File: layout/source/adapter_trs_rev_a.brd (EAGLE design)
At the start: 200 x 50 mm, 81 parts, among them IC1 STM32F103C8T, IC2 LP2985-SOT23-5, IC3 IC_USBLC6-2, IC4 IC_USBLC6-2, IC5 LT1619ES8, IC6 LP2985-SOT23-5, IC7 IRF7470, SW1 2P2T, T1 LPISR, Y1 532-CRYSTAL, Y2 EQ161-CRYSTAL

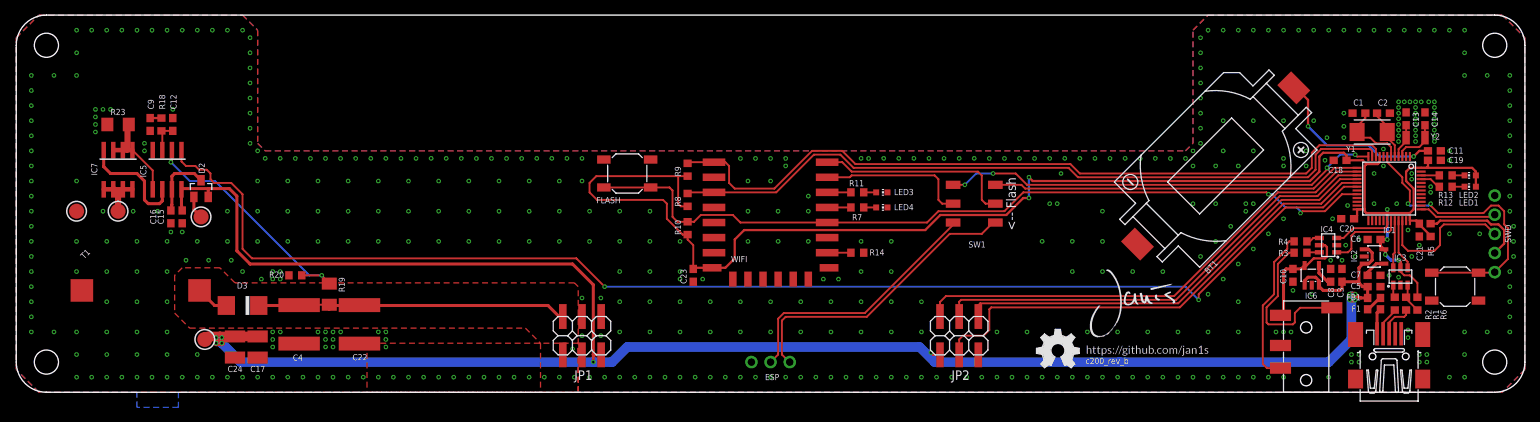
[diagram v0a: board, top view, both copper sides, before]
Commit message: Added new control board versions and TRS adapter
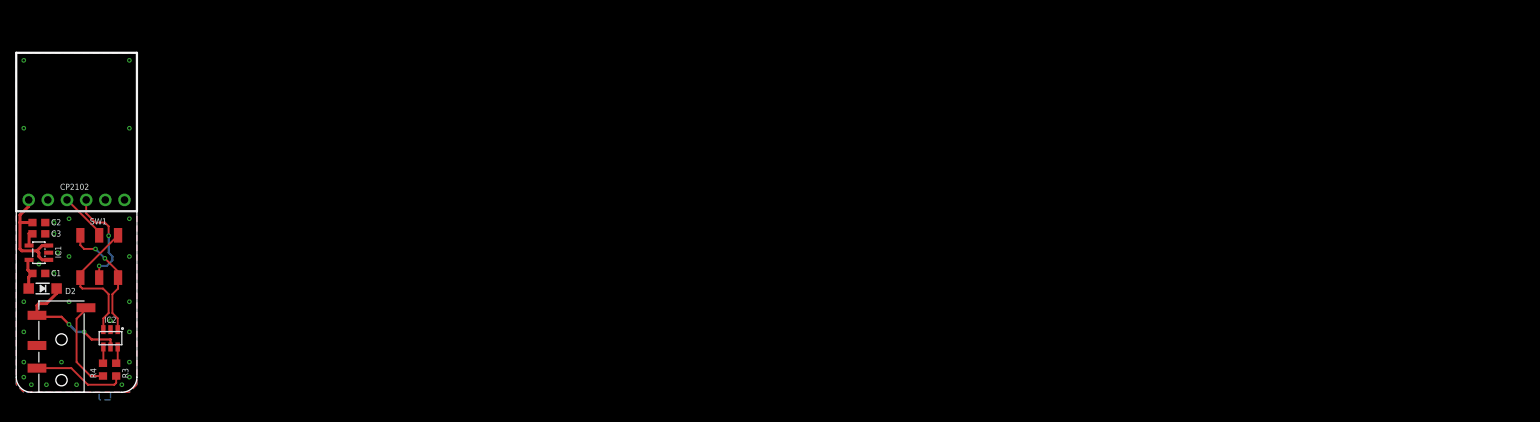
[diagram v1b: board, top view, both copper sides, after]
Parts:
- removed BT1: CR2032-HOLDER, battery-holder:CH28-2032LF
- removed C10, C11, C5, C6: 10µF/6.3V, rcl:C0603
- removed C12: 22nF, rcl:C0603
- removed C13, C14: 10p, rcl:C0603
- removed C15, C16: 10µF, rcl:C0603
- removed C17, C24: 100µF/6.3V, rcl:C1210
- removed C18, C23: 1µF, rcl:C0603
- removed C19, C20, C21: 100nF, rcl:C0603
- removed C22, C4: 1µF/250V, rcl:C2220K
- removed C7, C8: 10nF, rcl:C0603
- removed C9: 150pF, rcl:C0603
- removed D3: ES2, diode:DO-214AA
- removed ESP: (no value), microbuilder:1X03_ROUND
- removed F1, R12, R13: 1k, rcl:R0603
- removed FB1: EMI, rcl:R0603
- removed FLASH, ISP: TACT-SWITCH-40-40, tactile-switch:40-40
- removed IC3, IC4: IC_USBLC6-2, dp_devices:SOT-23-6L
- removed IC5: LT1619ES8, lt:SO8
- removed IC6: LP2985-SOT23-5, vreg:SOT23-5
- removed IC7: IRF7470, ir:SO8
- removed JP1, JP2: (no value), con-pinhead:2X03SMD
- removed LED1, LED2, LED3, LED4: (no value), led:CHIP-LED0603
- removed LOGO1, LOGO2: OSHW_LOGO_FILLX0200-NT, ohw-logo:OSHW_FILLX200_NOTEXT
- removed R1, R2, R5: 33R, rcl:R0603
- removed R10, R11, R14, R7, R8, R9: 10k, rcl:R0603
- removed R18: 82k, rcl:R0603
- removed R19: 1M, rcl:M1206
- removed R20: 8k2, rcl:R0603
- removed R23: 0.01R, rcl:R1206
- removed R6: 1k5, rcl:R0603
- removed SWD: (no value), microbuilder:1X05_ROUND
- removed T1: LPISR, fastron:PISR
- removed TP1, TP2, TP3, TP4: (no value), microbuilder:TESTPOINT_ROUND_2MM
- removed U$5: (no value), pcb-artwork:GITHUB/JAN1S
- removed WIFI: ESP-12F, espressif:ESP-12F
- removed X1: (no value), con-cypressindustries:32005-201
- removed Y1: 532-CRYSTAL, euroquartz:2PIN50X32
- removed Y2: EQ161-CRYSTAL, euroquartz:EQ161
- added CP2102: (no value), microbuilder:1X06_ROUND
- C1, C2: value 10p -> 1µF
- C3: value 10µF/6.3V -> 10nF/NP
- D2: value BAT54C -> 1n5819/SOD123; device diode:SOT23 -> microbuilder:SOD-123
- IC1: value STM32F103C8T -> LP2985-SOT23-5; device micro-stm_v3:LQFP48 -> vreg:SOT23-5
- IC2: value LP2985-SOT23-5 -> IC_USBLC6-2; device vreg:SOT23-5 -> dp_devices:SOT-23-6L
- U$1: device pcb-artwork:JANIS_10MM -> ohw-logo:OSHW_FILLX150_NOTEXT
- moved IC1 179.2 mm to (3.00, 18.5), turned to 90 degrees
- moved C2 178.8 mm to (3.00, 22.5)
- moved C1 176.3 mm to (3.00, 15.8), turned to 0 degrees
- moved C3 172.8 mm to (3.00, 21.0), turned to 0 degrees
- moved IC2 167.9 mm to (12.5, 6.00), turned to 180 degrees
- moved TRS1 165.0 mm to (6.00, 0.00)
- moved R4 159.7 mm to (11.5, 3.00), turned to 90 degrees
- moved R3 157.8 mm to (13.2, 3.00), turned to 90 degrees
- moved U$1 127.0 mm to (15.0, 5.00), flipped to the bottom, turned to 270 degrees
- moved SW1 116.2 mm to (11.0, 18.0), turned to 0 degrees
- moved U$2 94.6 mm to (11.8, 19.5), turned to 270 degrees
- moved U$6 94.5 mm to (13.8, 22.0), turned to 270 degrees
- moved D2 24.8 mm to (3.50, 13.8), turned to 180 degrees
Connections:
- removed net ASDAWJIODJA: R5.1, SWD.4
- removed net HV: C22.1, C4.1, D3.C, JP1.2, R19.2
- removed net HV_EN: IC1.18, IC5.1
- removed net I2C1_SCL: IC1.42
- removed net I2C1_SDA: IC1.43
- removed net I2C2_SCL: IC1.21
- removed net I2C2_SDA: IC1.22
- removed net JNTRST: IC1.40
- removed net JTDI: IC1.38
- removed net JTDO: IC1.39
- removed net LED_BOOT: IC1.46, R13.1
- removed net LED_FIX: IC1.45, R12.1
- removed net N$10: LED2.C, R13.2
- removed net N$11: LED1.C, R12.2
- removed net N$12: R4.1, TRS1.2
- removed net N$13: IC7.5, IC7.6, IC7.7, IC7.8, TP2.P$1
- removed net N$14: C12.1, IC5.3, R18.1
- removed net N$15: C9.1, R18.2
- removed net N$16: D3.A, T1.P$1
- removed net N$17: IC5.2, R19.1, R20.1
- removed net N$18: IC5.5, IC7.1, IC7.2, IC7.3, R23.2
- removed net N$19: C16.1, D2.3, IC5.7
- removed net N$20: C7.1, IC2.4
- removed net N$21: SW1.C1, WIFI.22
- removed net N$22: F1.2, FB1.2
- removed net N$23: IC3.1, R2.2
- removed net N$24: R2.1, X1.2
- removed net N$26: SW1.C2, WIFI.21
- removed net N$27: R11.1, WIFI.20
- removed net N$28: R3.1, TRS1.5
- removed net N$29: C13.1, IC1.4, Y2.P$1
- removed net N$3: F1.1, X1.1
- removed net N$30: C14.1, IC1.3, Y2.P$2
- removed net N$31: ESP.3, SW1.B1
- removed net N$32: ESP.2, SW1.B2
- removed net N$33: R7.1, WIFI.19
- removed net N$34: LED4.A, R7.2
- removed net N$35: LED3.A, R11.2
- removed net N$36: R1.1, X1.3
- removed net N$38: IC1.29
- removed net N$48: IC1.41
- removed net N$5: IC3.3, R1.2, R6.2
- removed net N$55: IC1.25
- removed net NX_EN: IC1.14, JP2.2
- removed net NX_RCK: IC1.16, JP2.6
- removed net RESET: IC1.7, ISP.3, ISP.4, SWD.5
- removed net RFMOD_DBG: IC1.19
- removed net RFMOD_EN: IC1.11, R8.1, WIFI.3
- removed net RFMOD_FLASH: FLASH.3, FLASH.4, IC1.20, R10.1, WIFI.18
- removed net RFMOD_RST: IC1.10, R9.1, WIFI.1
- removed net RTC-TAMPER: IC1.2
- removed net SPI1_MOSI: IC1.17, JP2.3
- removed net SPI1_SCK: IC1.15, JP2.4
- removed net SPI2_MISO: IC1.27
- removed net SPI2_MOSI: IC1.28
- removed net SPI2_SCK: IC1.26
- removed net SWCLK: IC1.37, SWD.2
- removed net SWDIO: IC1.34, SWD.3
- removed net TRS_VCC: C10.1, IC4.5, IC6.5, TRS1.4
- removed net USART2_RX: IC1.13, SW1.A1
- removed net USART2_TX: IC1.12, SW1.A2
- removed net USB_DM: IC1.32, IC3.6
- removed net USB_DP: IC1.33, IC3.4
- removed net VBAT: BT1.POS, C11.1, IC1.1
- net +3V3: now also D2.C, TRS1.4; no longer C18.1, C19.1, C20.1, C21.1, C23.1, C6.1, IC1.24, IC1.36, IC1.48, IC1.9, IC3.5, LED1.A, LED2.A, R10.2, R5.2, R6.1, R8.2, R9.2, WIFI.8
- net +5V: now also C2.1, CP2102.1, IC1.1, IC1.3; no longer C15.1, C17.1, C24.1, C3.1, C5.1, D2.2, FB1.1, IC2.1, IC2.3, IC5.8, IC6.1, IC6.3, JP1.5, JP2.1, TP1.P$1
- net GND: now also CP2102.2, IC1.2; no longer BT1.NEG, C10.2, C11.2, C12.2, C13.2, C14.2, C15.2, C16.2, C17.2, C18.2, C19.2, C20.2, C21.2, C22.2, C23.2, C24.2, C4.2, C5.2, C6.2, C7.2, C8.2, C9.2, ESP.1, FLASH.1, FLASH.2, IC1.23, IC1.35, IC1.44, IC1.47, IC1.8, IC3.2, IC4.2, IC5.4, IC6.2, ISP.1, ISP.2, JP1.1, JP1.3, JP1.4, JP1.6, JP2.5, LED3.C, LED4.C, R14.2, R20.2, R23.1, SWD.1, T1.P$2, TP4.P$1, WIFI.15, X1.5, X1.M1, X1.M2, X1.M3, X1.M4
- net N$1: now also D2.A, IC1.5; no longer IC1.6, Y1.P$1
- net N$2: now also C3.1, IC1.4; no longer C2.1, IC1.5, Y1.P$2
- net N$25: now also IC2.4; no longer IC4.4
- net N$4: now also R3.1, TRS1.2; no longer C8.1, IC6.4
- net N$6: now also CP2102.3, SW1.C1; no longer R14.1, WIFI.16
- net N$7: now also IC2.6; no longer IC4.6
- net N$8: now also R4.1, TRS1.5; no longer D2.1, TP3.P$1
- net N$9: now also CP2102.4, SW1.C2; no longer IC5.6, IC7.4
- net USART1_RX: now also IC2.1, SW1.A1, SW1.B2; no longer IC1.31, IC4.1
- net USART1_TX: now also IC2.3, SW1.A2, SW1.B1; no longer IC1.30, IC4.3
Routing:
- net +5V: track 300.7 -> 15.2 mm, vias 10 -> 0
- net +3V3: track 199.5 -> 18.1 mm, vias 6 -> 2
- net HV_EN: track 176.3 -> 0.00 mm, vias 2 -> 0
- net RFMOD_FLASH: track 108.5 -> 0.00 mm, vias 2 -> 0
- net RFMOD_RST: track 101.3 -> 0.00 mm
- net RFMOD_EN: track 97.7 -> 0.00 mm
- net SPI1_MOSI: track 65.0 -> 0.00 mm
- net NX_EN: track 64.4 -> 0.00 mm
- net SPI1_SCK: track 61.6 -> 0.00 mm
- net NX_RCK: track 58.7 -> 0.00 mm
- net USART2_TX: track 58.2 -> 0.00 mm, vias 4 -> 0
- net USART2_RX: track 49.3 -> 0.00 mm
- net HV: track 42.9 -> 0.00 mm
- net N$31: track 39.6 -> 0.00 mm
- net RESET: track 39.3 -> 0.00 mm, vias 2 -> 0
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- removed copper zone on layer 1, net +5V
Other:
- board size 200 x 50 mm -> 16 x 45 mm
- board text removed: "<-- Flash"
- board text removed: "GND"
- board text removed: "RST"
- board text removed: "RX"
- board text removed: "SWCLK"
- board text removed: "SWDIO"
- board text removed: "TX"
- board text removed: "VCC"
- board text removed: "c200_rev_b"
